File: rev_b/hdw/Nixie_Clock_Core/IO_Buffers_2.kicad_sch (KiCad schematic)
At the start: 17 parts, among them U2901 TCA9803, U2902 74VHC541

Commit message: lots of rev B control board schematic progress
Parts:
- removed R2907, R2908, R2909, R2910, R2911, R2912: 1k, Resistors_SMD:R_0603, symbol Custom_Library:R_Custom
- removed RN2901: 10k, Resistors_SMD:R_Array_Convex_8x0602, symbol Device:R_Pack08
- renumbered RN2902 to RN?, U2902 to U?, U2901 to U?
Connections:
- net +5V is gone; now on net +3.3V: C?.1, C?.1, U?.8 (VCCB)
- net ~{Display_Detect_DSP}: now also RN?.9 (R8.2), U?.9 (A7)
- net Pushbutton_0: now reaches RN?.16 (R1.2), U?.2 (A0)
- net Pushbutton_1: now reaches RN?.15 (R2.2), U?.3 (A1)
- net Pushbutton_2: now reaches RN?.14 (R3.2), U?.4 (A2)
- net Pushbutton_3: now reaches RN?.13 (R4.2), U?.5 (A3)
- net Pushbutton_4: now reaches RN?.12 (R5.2), U?.6 (A4)
- net Pushbutton_5: now reaches RN?.11 (R6.2), U?.7 (A5)
- net Pushbutton_6: now reaches RN?.10 (R7.2), U?.8 (A6)
- net Cap_Touch_Down: no longer names the net of U?.15 (Y3)
- net Cap_Touch_Left: no longer names the net of U?.18 (Y0)
- net Cap_Touch_Power: no longer names the net of U?.14 (Y4)
- net Cap_Touch_Right: no longer names the net of U?.17 (Y1)
- net Cap_Touch_Up: no longer names the net of U?.16 (Y2)
- net ~{Display_Detect}: no longer names the net of U?.13 (Y5)

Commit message: more rev b sch progress
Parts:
- added R? (x3): 10K, Resistors_SMD:R_0603, symbol Custom_Library:R_Custom
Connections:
- net +3.3V: now also R?.1, R?.1, R?.1
- net I2C_DSP_SCL: now also R?.2
- net I2C_DSP_SDA: now also R?.2
- net ~{Display_Detect_DSP}: no longer RN?.9 (R8.2)
- net ~{IO_Level_Shift_Enable}: now also R?.2
- net Pushbutton_0 renamed Pushbutton_0_DSP
- net Pushbutton_1 renamed Pushbutton_1_DSP
- net Pushbutton_2 renamed Pushbutton_2_DSP
- net Pushbutton_3 renamed Pushbutton_3_DSP
- net Pushbutton_4 renamed Pushbutton_4_DSP
- net Pushbutton_5 renamed Pushbutton_5_DSP
- net Pushbutton_6 renamed Pushbutton_6_DSP
- no-connect marks 0 -> 1
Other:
- moved on the sheet: C?, R?, RN?, U?

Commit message: more carrier board progress
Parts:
- added R? (x2): 10K, Resistors_SMD:R_0603, symbol Custom_Library:R_Custom
- added RN?: 10k, Resistors_SMD:R_Array_Convex_8x0602, symbol Device:R_Pack08
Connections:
- net +3.3V: now also R?.1, R?.1; no longer RN?.6 (R6.1)
- net GND: now also RN?.6 (R6.1), RN?.1 (R1.1), RN?.2 (R2.1), RN?.3 (R3.1), RN?.4 (R4.1), RN?.5 (R5.1), RN?.6 (R6.1), RN?.7 (R7.1), RN?.8 (R8.1)
- net ~{Display_Detect_DSP}: now also R?.2
- net ~{Display_Detect}: now reaches U?.11 (Y7)
- net ~{Display_Detect}: now also R?.2
- net Pushbutton_6: now reaches U?.12 (Y6)
- net Pushbutton_6: now also RN?.10 (R7.2)
- net Pushbutton_5: now reaches U?.13 (Y5)
- net Pushbutton_5: now also RN?.11 (R6.2)
- net Pushbutton_4: now reaches U?.14 (Y4)
- net Pushbutton_4: now also RN?.12 (R5.2)
- net Pushbutton_3: now reaches U?.15 (Y3)
- net Pushbutton_3: now also RN?.13 (R4.2)
- net Pushbutton_2: now reaches U?.16 (Y2)
- net Pushbutton_2: now also RN?.14 (R3.2)
- net Pushbutton_1: now reaches U?.17 (Y1)
- net Pushbutton_1: now also RN?.15 (R2.2)
- net Pushbutton_0: now reaches U?.18 (Y0)
- net Pushbutton_0: now also RN?.16 (R1.2)
- no-connect marks 1 -> 2
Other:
- moved on the sheet: RN?

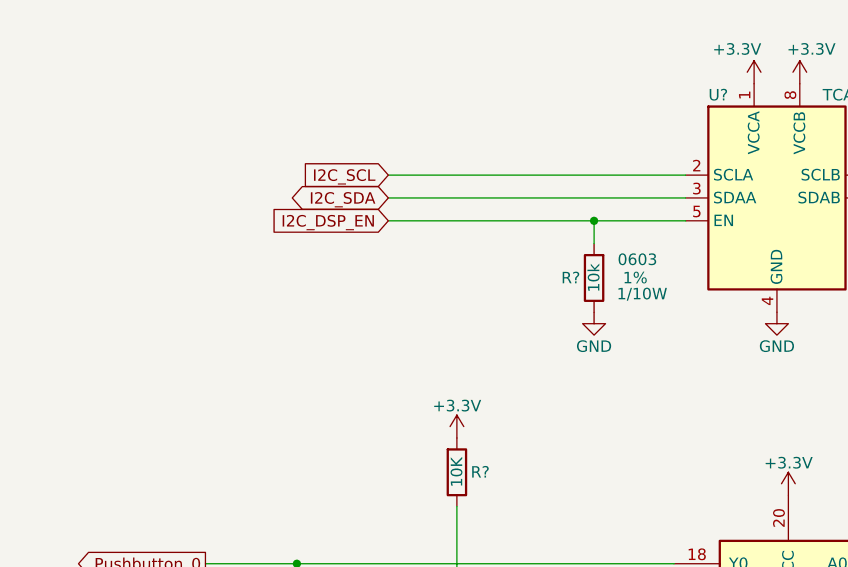
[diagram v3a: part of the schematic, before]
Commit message: more schematic progress, assigning signals to MCU"
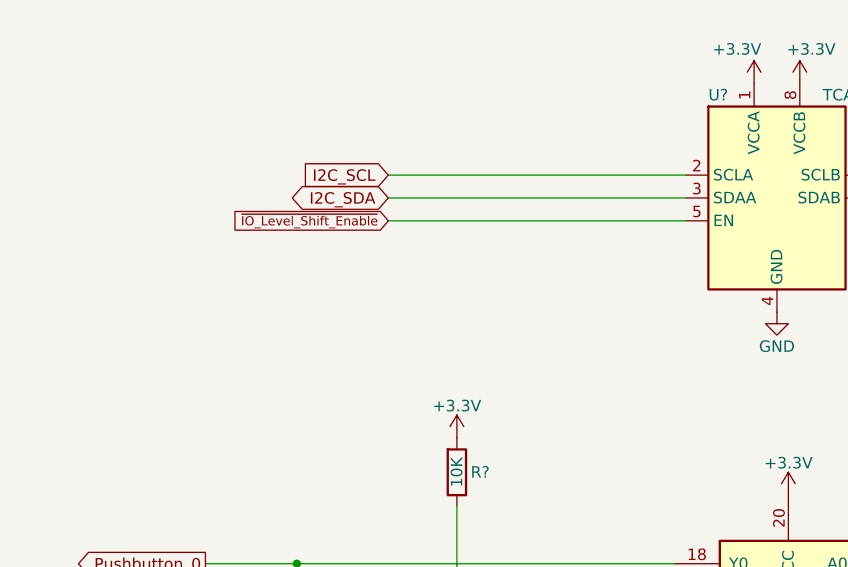
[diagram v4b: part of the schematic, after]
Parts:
- removed R?: 10k, Resistors_SMD:R_0603, symbol Custom_Library:R_Custom
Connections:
- net I2C_DSP_EN is gone; now on net ~{IO_Level_Shift_Enable}: U?.5 (EN)
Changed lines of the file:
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@@
   (junction (at 184.15 106.68) (diameter 0) (color 0 0 0 0)
-  )
-  (junction (at 107.95 68.58) (diameter 0) (color 0 0 0 0)
   )
   (junction (at 87.63 119.38) (diameter 0) (color 0 0 0 0)
@@
     (stroke (width 0) (type default))
   )
+  (wire (pts (xy 85.09 68.58) (xy 118.11 68.58))
+    (stroke (width 0) (type default))
+  )
   (wire (pts (xy 64.77 111.76) (xy 80.01 111.76))
     (stroke (width 0) (type default))
@@
     (stroke (width 0) (type default))
   )
-  (wire (pts (xy 85.09 68.58) (xy 107.95 68.58))
-    (stroke (width 0) (type default))
-  )
   (wire (pts (xy 87.63 134.62) (xy 87.63 119.38))
     (stroke (width 0) (type default))
@@
     (stroke (width 0) (type default))
   )
-  (wire (pts (xy 118.11 68.58) (xy 107.95 68.58))
-    (stroke (width 0) (type default))
-  )
   (wire (pts (xy 171.45 144.78) (xy 171.45 146.05))
     (stroke (width 0) (type default))
@@
   )
   (wire (pts (xy 171.45 146.05) (xy 173.99 146.05))
-    (stroke (width 0) (type default))
-  )
-  (wire (pts (xy 107.95 68.58) (xy 107.95 71.12))
     (stroke (width 0) (type default))
   )
@@
     )
   )
-  (global_label "I2C_DSP_EN" (shape input) (at 85.09 68.58 180)
-    (effects (font (size 1.27 1.27)) (justify right))
+  (global_label "Pushbutton_6_DSP" (shape input) (at 194.31 121.92 0) (fields_autoplaced)
+    (effects (font (size 1.27 1.27)) (justify left))
+    (property "Intersheetrefs" "${INTERSHEET_REFS}" (at 214.7535 121.92 0)
+      (effects (font (size 1.27 1.27)) (justify left) hide)
+    )
+  )
+  (global_label "~{IO_Level_Shift_Enable}" (shape input) (at 85.09 68.58 180)
+    (effects (font (size 1.016 1.016)) (justify right))
     (property "Intersheetrefs" "${INTERSHEET_REFS}" (at 85.09 68.58 0)
       (effects (font (size 1.27 1.27)) hide)
-    )
-  )
-  (global_label "Pushbutton_6_DSP" (shape input) (at 194.31 121.92 0) (fields_autoplaced)
-    (effects (font (size 1.27 1.27)) (justify left))
-    (property "Intersheetrefs" "${INTERSHEET_REFS}" (at 214.7535 121.92 0)
-      (effects (font (size 1.27 1.27)) (justify left) hide)
     )
   )
@@
         (path "/16fdce21-b570-4d81-a458-e8839d611806/8bfc37a9-2570-4706-99e7-147636a5a42e"
           (reference "#PWR?") (unit 1)
-        )
-      )
-    )
-  )
-  (symbol (lib_id "Custom_Library:R_Custom") (at 107.95 74.93 0) (unit 1)
-    (in_bom yes) (on_board yes) (dnp no)
-    (property "Reference" "R?" (at 106.426 74.93 0)
-      (effects (font (size 1.27 1.27)) (justify right))
-    )
-    (property "Value" "10k" (at 107.95 74.93 90)
-      (effects (font (size 1.27 1.27)))
-    )
-    (property "Footprint" "Resistors_SMD:R_0603" (at 107.95 74.93 0)
-      (effects (font (size 1.27 1.27)) hide)
-    )
-    (property "Datasheet" "" (at 107.95 74.93 0)
-      (effects (font (size 1.27 1.27)) hide)
-    )
-    (property "display_footprint" "0603" (at 112.776 72.898 0)
-      (effects (font (size 1.27 1.27)))
-    )
-    (property "Tolerance" "1%" (at 112.522 74.93 0)
-      (effects (font (size 1.27 1.27)))
-    )
-    (property "Wattage" "1/10W" (at 113.284 76.708 0)
-      (effects (font (size 1.27 1.27)))
-    )
-    (property "Digi-Key PN" "RMCF0603FT10K0CT-ND" (at 115.57 64.77 0)
-      (effects (font (size 1.524 1.524)) hide)
-    )
-    (pin "1")
-    (pin "2")
-    (instances
-      (project "VFD_Clock"
-        (path "/0e0fa043-3ab8-4cb9-8105-f968ef03a597/00000000-0000-0000-0000-00005baae1dc"
-          (reference "R?") (unit 1)
-        )
-        (path "/0e0fa043-3ab8-4cb9-8105-f968ef03a597/00000000-0000-0000-0000-00005bb844fd"
-          (reference "R?") (unit 1)
-        )
-        (path "/0e0fa043-3ab8-4cb9-8105-f968ef03a597/00000000-0000-0000-0000-00005cb0bc26"
-          (reference "R?") (unit 1)
-        )
-        (path "/0e0fa043-3ab8-4cb9-8105-f968ef03a597/00000000-0000-0000-0000-00005cc31b3e"
-          (reference "R?") (unit 1)
-        )
-        (path "/0e0fa043-3ab8-4cb9-8105-f968ef03a597/00000000-0000-0000-0000-00005baae16c"
-          (reference "R?") (unit 1)
-        )
-        (path "/0e0fa043-3ab8-4cb9-8105-f968ef03a597/00000000-0000-0000-0000-00005e0cf7bc"
-          (reference "R?") (unit 1)
-        )
-        (path "/0e0fa043-3ab8-4cb9-8105-f968ef03a597/00000000-0000-0000-0000-00005c1d5cb6"
-          (reference "R?") (unit 1)
-        )
-        (path "/0e0fa043-3ab8-4cb9-8105-f968ef03a597/00000000-0000-0000-0000-00005baae1f3"
-          (reference "R?") (unit 1)
-        )
-      )
-      (project "Nixie_Clock_Core"
-        (path "/16fdce21-b570-4d81-a458-e8839d611806/8bfc37a9-2570-4706-99e7-147636a5a42e"
-          (reference "R?") (unit 1)
         )
       )
@@
         )
       )
-    )
-  )
-  (symbol (lib_id "power:GND") (at 107.95 78.74 0) (unit 1)
-    (in_bom yes) (on_board yes) (dnp no)
-    (property "Reference" "#PWR?" (at 107.95 85.09 0)
-      (effects (font (size 1.27 1.27)) hide)
-    )
-    (property "Value" "GND" (at 107.95 82.55 0)
-      (effects (font (size 1.27 1.27)))
-    )
-    (property "Footprint" "" (at 107.95 78.74 0)
-      (effects (font (size 1.27 1.27)) hide)
-    )
-    (property "Datasheet" "" (at 107.95 78.74 0)
-      (effects (font (size 1.27 1.27)) hide)
-    )
-    (pin "1")
-    (instances
-      (project "VFD_Clock"
-        (path "/0e0fa043-3ab8-4cb9-8105-f968ef03a597/00000000-0000-0000-0000-00005cc31b3e"
-          (reference "#PWR?") (unit 1)
-        )
-        (path "/0e0fa043-3ab8-4cb9-8105-f968ef03a597/00000000-0000-0000-0000-00005e0cf7bc"
-          (reference "#PWR?") (unit 1)
-        )
-      )
-      (project "Nixie_Clock_Core"
-        (path "/16fdce21-b570-4d81-a458-e8839d611806/8bfc37a9-2570-4706-99e7-147636a5a42e"
-          (reference "#PWR?") (unit 1)
-        )
-      )

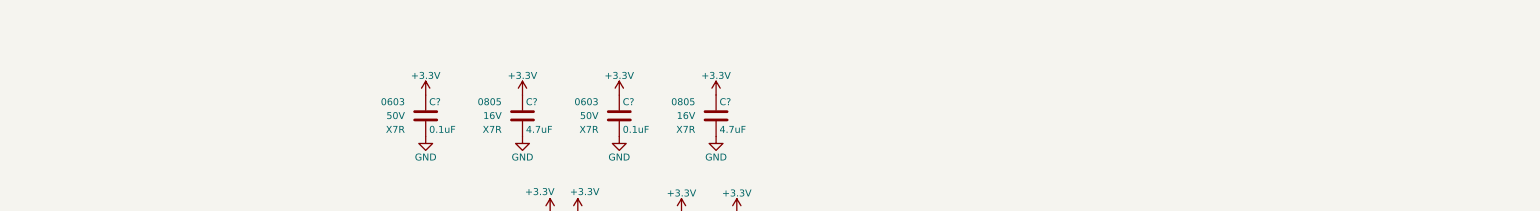
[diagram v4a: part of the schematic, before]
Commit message: updated footprints, ran some DRC
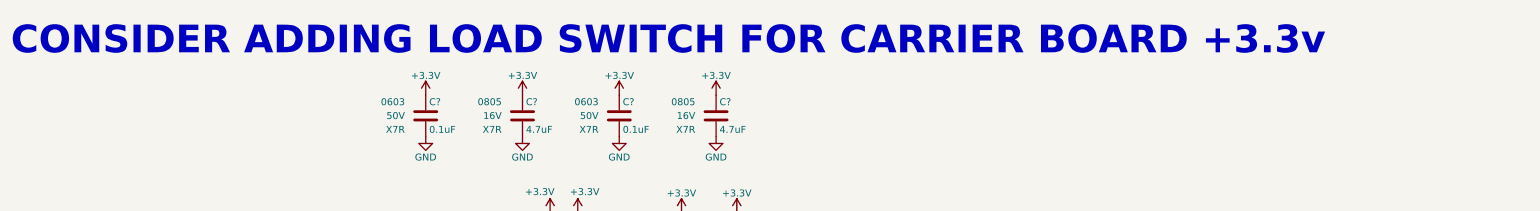
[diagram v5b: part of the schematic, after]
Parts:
- C? (x2): Digi-Key PN 1276-2970-1-ND -> (none)
- C? (x3): Digi-Key PN 311-1344-1-ND -> (none)
- R? (x6): Digi-Key PN RHM10KADCT-ND -> (none)
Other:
- note added: "CONSIDER ADDING LOAD SWITCH FOR CARRIER BOARD +3.3v"
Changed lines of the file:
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@@
     (stroke (width 0) (type default))
+  )
+  (text "CONSIDER ADDING LOAD SWITCH FOR CARRIER BOARD +3.3v"
+    (at 26.67 24.765 0)
+    (effects (font (face "Courier New") (size 5.08 5.08) (thickness 0.254) bold (color 255 37 56 1)) (justify left bottom))
   )
   (global_label "Pushbutton_2" (shape output) (at 64.77 111.76 180) (fields_autoplaced)
@@
       (project "Nixie_Clock_Core"
         (path "/16fdce21-b570-4d81-a458-e8839d611806/8bfc37a9-2570-4706-99e7-147636a5a42e"
-          (reference "#PWR?") (unit 1)
+          (reference "#PWR01821") (unit 1)
         )
       )
@@
       (project "Nixie_Clock_Core"
         (path "/16fdce21-b570-4d81-a458-e8839d611806/8bfc37a9-2570-4706-99e7-147636a5a42e"
-          (reference "#PWR?") (unit 1)
+          (reference "#PWR01820") (unit 1)
         )
       )
@@
       (effects (font (size 1.27 1.27)) (justify right))
     )
-    (property "Digi-Key PN" "1276-2970-1-ND" (at 6.35 151.384 0)
+    (property "Digi-Key PN" "" (at 6.35 151.384 0)
       (effects (font (size 1.27 1.27)) hide)
     )
@@
       (project "Nixie_Clock_Core"
         (path "/16fdce21-b570-4d81-a458-e8839d611806/8bfc37a9-2570-4706-99e7-147636a5a42e"
-          (reference "C?") (unit 1)
+          (reference "C1805") (unit 1)
         )
       )
@@
       (project "Nixie_Clock_Core"
         (path "/16fdce21-b570-4d81-a458-e8839d611806/8bfc37a9-2570-4706-99e7-147636a5a42e"
-          (reference "#PWR?") (unit 1)
+          (reference "#PWR01816") (unit 1)
         )
       )
@@
       (project "Nixie_Clock_Core"
         (path "/16fdce21-b570-4d81-a458-e8839d611806/8bfc37a9-2570-4706-99e7-147636a5a42e"
-          (reference "#PWR?") (unit 1)
+          (reference "#PWR01822") (unit 1)
         )
       )
@@
       (effects (font (size 1.27 1.27)) (justify left) hide)
     )
-    (property "Digi-Key PN" "RHM10KADCT-ND" (at 163.83 86.36 0)
+    (property "Digi-Key PN" "" (at 163.83 86.36 0)
       (effects (font (size 1.524 1.524)) hide)
     )
@@
       (project "Nixie_Clock_Core"
         (path "/16fdce21-b570-4d81-a458-e8839d611806/8bfc37a9-2570-4706-99e7-147636a5a42e"
-          (reference "R?") (unit 1)
+          (reference "R1804") (unit 1)
         )
       )
@@
       (project "Nixie_Clock_Core"
         (path "/16fdce21-b570-4d81-a458-e8839d611806/8bfc37a9-2570-4706-99e7-147636a5a42e"
-          (reference "U?") (unit 1)
+          (reference "U1802") (unit 1)
         )
       )
@@
       (project "Nixie_Clock_Core"
         (path "/16fdce21-b570-4d81-a458-e8839d611806/8bfc37a9-2570-4706-99e7-147636a5a42e"
-          (reference "#PWR?") (unit 1)
+          (reference "#PWR01812") (unit 1)
         )
       )
@@
       (effects (font (size 1.27 1.27)) (justify right))
     )
-    (property "Digi-Key PN" "311-1344-1-ND" (at 149.225 22.86 0)
+    (property "Digi-Key PN" "" (at 149.225 22.86 0)
       (effects (font (size 1.524 1.524)) hide)
     )
@@
       (project "Nixie_Clock_Core"
         (path "/16fdce21-b570-4d81-a458-e8839d611806/8bfc37a9-2570-4706-99e7-147636a5a42e"
-          (reference "C?") (unit 1)
+          (reference "C1804") (unit 1)
         )
       )
@@
       (effects (font (size 1.27 1.27)) (justify right))
     )
-    (property "Digi-Key PN" "311-1344-1-ND" (at 113.665 22.86 0)
+    (property "Digi-Key PN" "" (at 113.665 22.86 0)
       (effects (font (size 1.524 1.524)) hide)
     )
@@
       (project "Nixie_Clock_Core"
         (path "/16fdce21-b570-4d81-a458-e8839d611806/8bfc37a9-2570-4706-99e7-147636a5a42e"
-          (reference "C?") (unit 1)
+          (reference "C1802") (unit 1)
         )
       )
@@
       (effects (font (size 1.27 1.27)) (justify left) hide)
     )
-    (property "Digi-Key PN" "RHM10KADCT-ND" (at 151.13 86.36 0)
+    (property "Digi-Key PN" "" (at 151.13 86.36 0)
       (effects (font (size 1.524 1.524)) hide)
     )
@@
       (project "Nixie_Clock_Core"
         (path "/16fdce21-b570-4d81-a458-e8839d611806/8bfc37a9-2570-4706-99e7-147636a5a42e"
-          (reference "R?") (unit 1)
+          (reference "R1802") (unit 1)
         )
       )
@@
       (project "Nixie_Clock_Core"
         (path "/16fdce21-b570-4d81-a458-e8839d611806/8bfc37a9-2570-4706-99e7-147636a5a42e"
-          (reference "#PWR?") (unit 1)
+          (reference "#PWR01817") (unit 1)
         )
       )
@@
       (project "Nixie_Clock_Core"
         (path "/16fdce21-b570-4d81-a458-e8839d611806/8bfc37a9-2570-4706-99e7-147636a5a42e"
-          (reference "RN?") (unit 1)
+          (reference "RN1801") (unit 1)
         )
       )
@@
       (project "Nixie_Clock_Core"
         (path "/16fdce21-b570-4d81-a458-e8839d611806/8bfc37a9-2570-4706-99e7-147636a5a42e"
-          (reference "#PWR?") (unit 1)
+          (reference "#PWR01813") (unit 1)
         )
       )
@@
       (project "Nixie_Clock_Core"
         (path "/16fdce21-b570-4d81-a458-e8839d611806/8bfc37a9-2570-4706-99e7-147636a5a42e"
-          (reference "#PWR?") (unit 1)
+          (reference "#PWR01815") (unit 1)
         )
       )
@@
       (effects (font (size 1.27 1.27)) (justify right))
     )
-    (property "Digi-Key PN" "311-1344-1-ND" (at 64.135 128.27 0)
+    (property "Digi-Key PN" "" (at 64.135 128.27 0)
       (effects (font (size 1.524 1.524)) hide)
     )
@@
       (project "Nixie_Clock_Core"
         (path "/16fdce21-b570-4d81-a458-e8839d611806/8bfc37a9-2570-4706-99e7-147636a5a42e"
-          (reference "C?") (unit 1)
+          (reference "C1801") (unit 1)
         )
       )
@@
       (project "Nixie_Clock_Core"
         (path "/16fdce21-b570-4d81-a458-e8839d611806/8bfc37a9-2570-4706-99e7-147636a5a42e"
-          (reference "U?") (unit 1)
+          (reference "U1801") (unit 1)
         )
       )
@@
       (project "Nixie_Clock_Core"
         (path "/16fdce21-b570-4d81-a458-e8839d611806/8bfc37a9-2570-4706-99e7-147636a5a42e"
-          (reference "#PWR?") (unit 1)
+          (reference "#PWR01823") (unit 1)
         )
       )
@@
       (project "Nixie_Clock_Core"
         (path "/16fdce21-b570-4d81-a458-e8839d611806/8bfc37a9-2570-4706-99e7-147636a5a42e"
-          (reference "#PWR?") (unit 1)
+          (reference "#PWR01818") (unit 1)
         )
       )
@@
       (effects (font (size 1.27 1.27)) (justify left) hide)
     )
-    (property "Digi-Key PN" "RHM10KADCT-ND" (at 158.75 86.36 0)
+    (property "Digi-Key PN" "" (at 158.75 86.36 0)
       (effects (font (size 1.524 1.524)) hide)
     )
@@
       (project "Nixie_Clock_Core"
         (path "/16fdce21-b570-4d81-a458-e8839d611806/8bfc37a9-2570-4706-99e7-147636a5a42e"
-          (reference "R?") (unit 1)
+          (reference "R1806") (unit 1)
         )
       )
@@
       (effects (font (size 1.27 1.27)) (justify left) hide)
     )
-    (property "Digi-Key PN" "RHM10KADCT-ND" (at 157.48 46.99 0)
+    (property "Digi-Key PN" "" (at 157.48 46.99 0)
       (effects (font (size 1.524 1.524)) hide)
     )
@@
       (project "Nixie_Clock_Core"
         (path "/16fdce21-b570-4d81-a458-e8839d611806/8bfc37a9-2570-4706-99e7-147636a5a42e"
-          (reference "R?") (unit 1)
+          (reference "R1803") (unit 1)
         )
       )
@@
       (effects (font (size 1.27 1.27)) (justify left) hide)
     )
-    (property "Digi-Key PN" "RHM10KADCT-ND" (at 85.09 86.36 0)
+    (property "Digi-Key PN" "" (at 85.09 86.36 0)
       (effects (font (size 1.524 1.524)) hide)
     )
@@
       (project "Nixie_Clock_Core"
         (path "/16fdce21-b570-4d81-a458-e8839d611806/8bfc37a9-2570-4706-99e7-147636a5a42e"
-          (reference "R?") (unit 1)
+          (reference "R1801") (unit 1)
         )
       )
@@
       (project "Nixie_Clock_Core"
         (path "/16fdce21-b570-4d81-a458-e8839d611806/8bfc37a9-2570-4706-99e7-147636a5a42e"
-          (reference "#PWR?") (unit 1)
+          (reference "#PWR01811") (unit 1)
         )
       )
@@
       (project "Nixie_Clock_Core"
         (path "/16fdce21-b570-4d81-a458-e8839d611806/8bfc37a9-2570-4706-99e7-147636a5a42e"
-          (reference "#PWR?") (unit 1)
+          (reference "#PWR01819") (unit 1)
         )
       )
@@
       (effects (font (size 1.27 1.27)) (justify left) hide)
     )
-    (property "Digi-Key PN" "RHM10KADCT-ND" (at 167.64 46.99 0)
+    (property "Digi-Key PN" "" (at 167.64 46.99 0)
       (effects (font (size 1.524 1.524)) hide)
     )
@@
       (project "Nixie_Clock_Core"
         (path "/16fdce21-b570-4d81-a458-e8839d611806/8bfc37a9-2570-4706-99e7-147636a5a42e"
-          (reference "R?") (unit 1)
+          (reference "R1805") (unit 1)
         )
       )
@@
       (project "Nixie_Clock_Core"
         (path "/16fdce21-b570-4d81-a458-e8839d611806/8bfc37a9-2570-4706-99e7-147636a5a42e"
-          (reference "#PWR?") (unit 1)
+          (reference "#PWR01814") (unit 1)
         )
       )
@@
       (project "Nixie_Clock_Core"
         (path "/16fdce21-b570-4d81-a458-e8839d611806/8bfc37a9-2570-4706-99e7-147636a5a42e"
-          (reference "RN?") (unit 1)
+          (reference "RN1802") (unit 1)
         )
       )
@@
       (project "Nixie_Clock_Core"
         (path "/16fdce21-b570-4d81-a458-e8839d611806/8bfc37a9-2570-4706-99e7-147636a5a42e"
-          (reference "#PWR?") (unit 1)
+          (reference "#PWR01810") (unit 1)
         )
       )
@@
       (effects (font (size 1.27 1.27)) (justify right))
     )
-    (property "Digi-Key PN" "1276-2970-1-ND" (at -29.21 151.384 0)
+    (property "Digi-Key PN" "" (at -29.21 151.384 0)
       (effects (font (size 1.27 1.27)) hide)
     )
@@
       (project "Nixie_Clock_Core"
         (path "/16fdce21-b570-4d81-a458-e8839d611806/8bfc37a9-2570-4706-99e7-147636a5a42e"
-          (reference "C?") (unit 1)
-        )
-      )
+          (reference "C1803") (unit 1)
+        )
+      )
